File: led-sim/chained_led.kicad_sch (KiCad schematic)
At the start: 5 parts, among them M1 2N7002

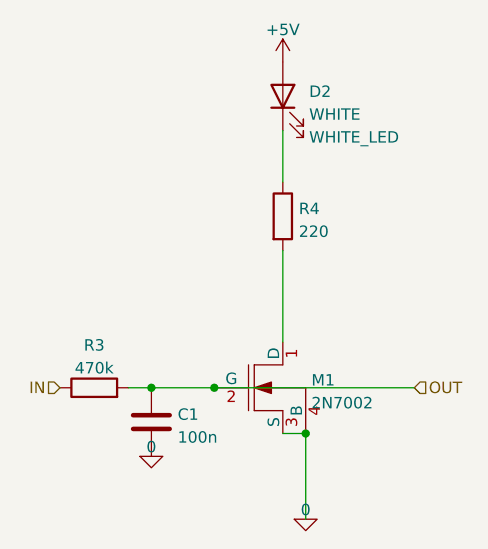
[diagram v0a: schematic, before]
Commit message: sim for LED timings with gate in between
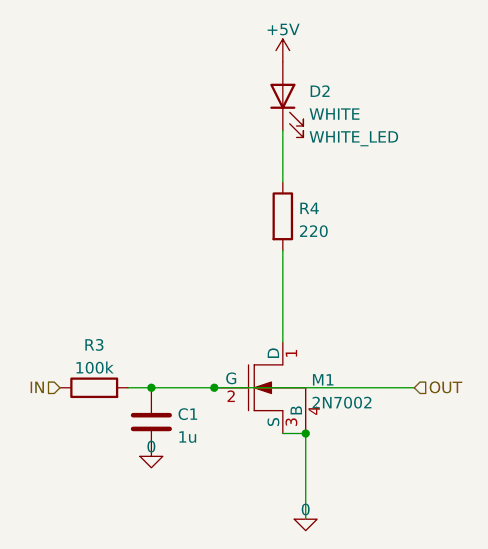
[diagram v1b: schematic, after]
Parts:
- C1: value 100n -> 1u
- R3: value 470k -> 100k
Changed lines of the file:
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@@
       (effects (font (size 1.27 1.27)) (justify left))
     )
-    (property "Value" "100n" (id 1) (at 42.291 66.4722 0)
+    (property "Value" "1u" (id 1) (at 42.291 66.4722 0)
       (effects (font (size 1.27 1.27)) (justify left))
     )
@@
     (in_bom yes) (on_board yes) (fields_autoplaced)
     (property "Reference" "R3" (id 0) (at 33.02 56.2442 90))
-    (property "Value" "470k" (id 1) (at 33.02 58.7811 90))
+    (property "Value" "100k" (id 1) (at 33.02 58.7811 90))
     (property "Footprint" "" (id 2) (at 33.02 62.738 90)
       (effects (font (size 1.27 1.27)) hide)
